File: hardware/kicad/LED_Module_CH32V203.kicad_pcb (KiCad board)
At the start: 2 copper layers, 40 x 40 mm, 97 parts, among them J1 USB_C_Receptacle_USB2.0_16P, J2 Solder Pad, J3 Qwiic / StemmaQT Connector, J4 noknok_FlashPads_USB-module, Q1 AO3401A, Q2 MMBT3904, U1 CH32V203G6U6, U2 BL9110-330BPFB (LCSC C169246), U3 SN74AHCT1G125DBVR (LCSC C7484), Y1 Crystal

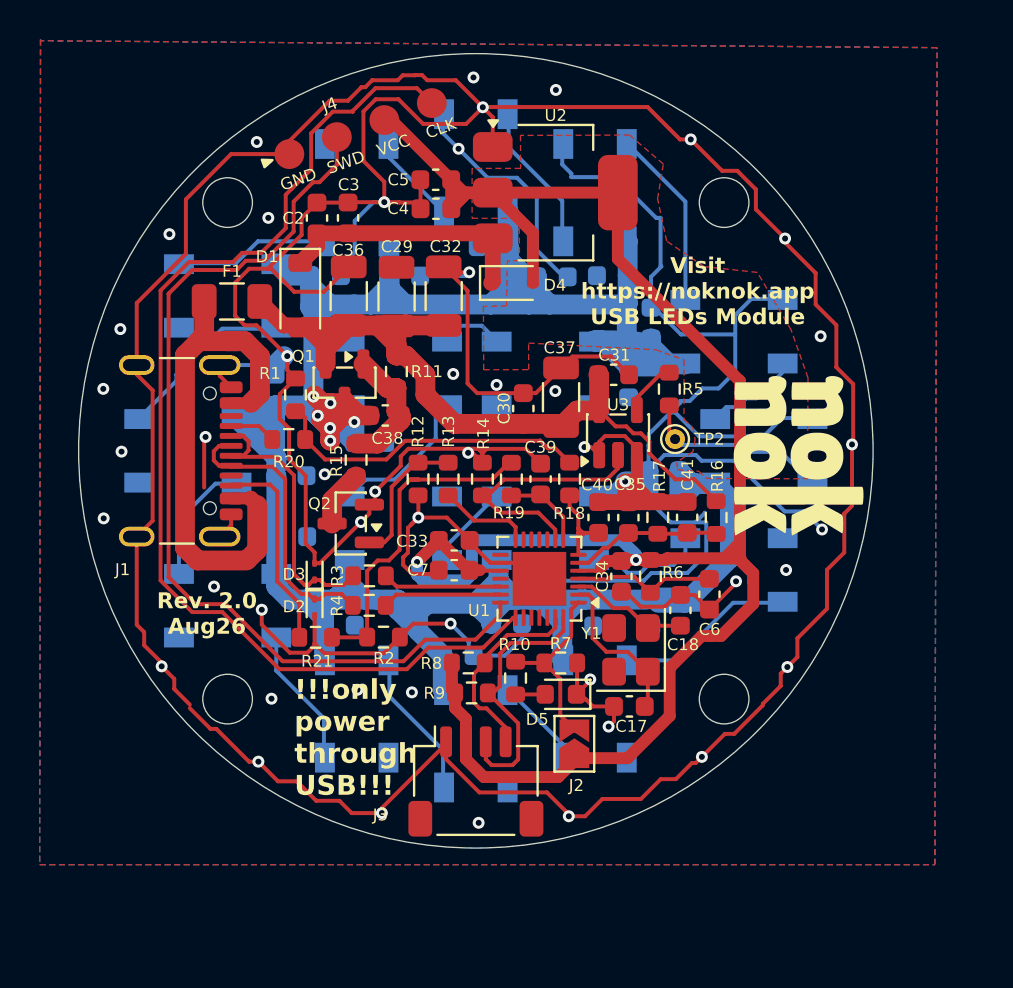
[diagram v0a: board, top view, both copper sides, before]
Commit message: hardware: revert to the 8x WS2812b board - the 16x SK6812 rev2 design moves to module-usb-led-16x
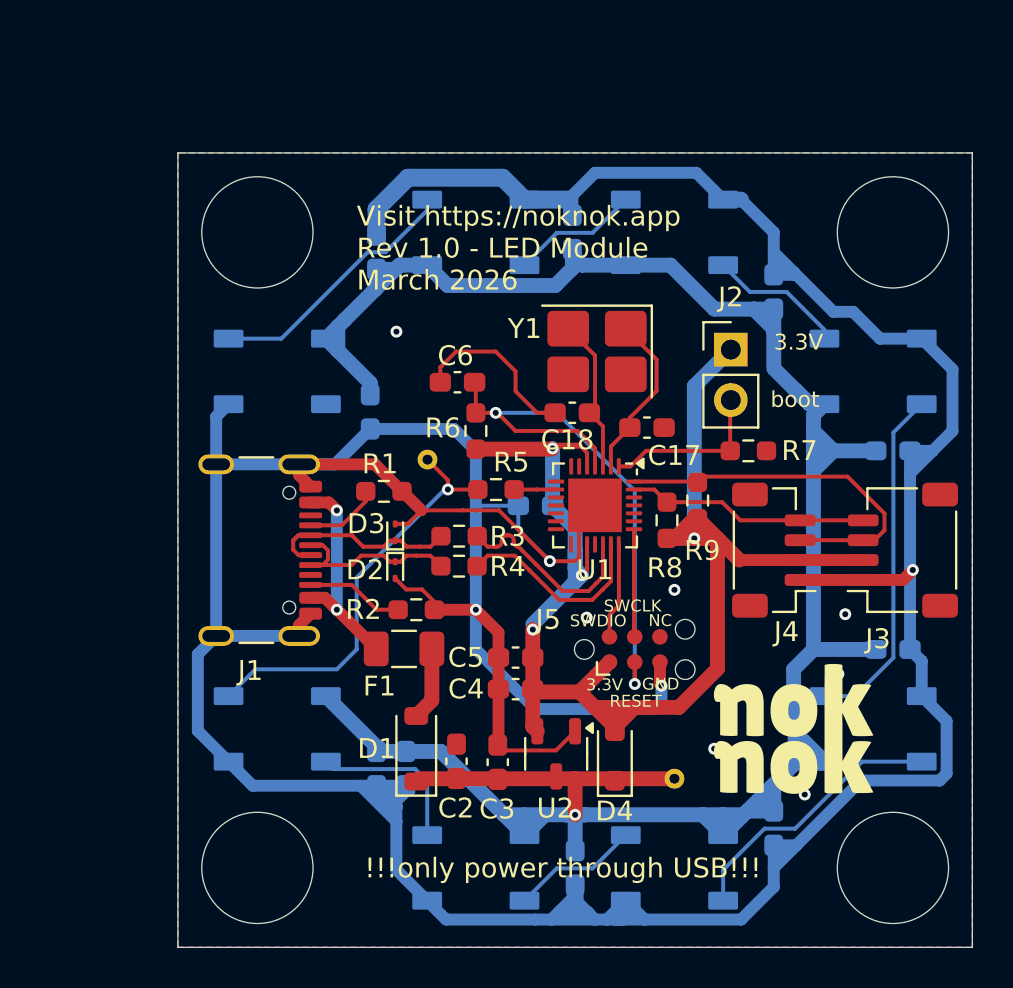
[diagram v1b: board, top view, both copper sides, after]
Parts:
- removed C19, C24: 10uF, Capacitor_SMD:C_0603_1608Metric
- removed C20, C21, C22, C23, C27, C28, C33, C34, C35, C38: 0.1uF, Capacitor_SMD:C_0603_1608Metric
- removed C29, C32, C36, C37: 22µF 25V X5R, Capacitor_SMD:C_1206_3216Metric
- removed C30, C39, C40, C41: 0.1uF X7R Ceramic, Capacitor_SMD:C_0603_1608Metric
- removed C31: 0.1uF X7R 16V+, Capacitor_SMD:C_0603_1608Metric
- removed D17, D18, D19, D20, D21, D22, D23, D24: SK6812, LED_SMD:LED_SK6812_PLCC4_5.0x5.0mm_P3.2mm
- removed D5: LED, LED_SMD:LED_0603_1608Metric
- removed H1, H2, H3: noknok_MountingHole, noknok:noknok_MountingHole_2.5mm_M2.5
- removed Q1: AO3401A, Package_TO_SOT_SMD:SOT-23
- removed Q2: MMBT3904, Package_TO_SOT_SMD:SOT-23
- removed R10: 2.2k, Resistor_SMD:R_0603_1608Metric
- removed R11, R12, R13, R14: 10k, Resistor_SMD:R_0603_1608Metric
- removed R15: 1k, Resistor_SMD:R_0603_1608Metric
- removed R16, R17: 22k, Resistor_SMD:R_0603_1608Metric
- removed R18, R19: 4.7k (1% tolerance), Resistor_SMD:R_0603_1608Metric
- removed R20, R21: 3.3k (1% tolerance), Resistor_SMD:R_0603_1608Metric
- removed U3: SN74AHCT1G125DBVR (LCSC C7484), Package_TO_SOT_SMD:SOT-23-5
- added J5: TagConnect_TC2030, Connector:Tag-Connect_TC2030-IDC-NL_2x03_P1.27mm_Vertical, F.Cu at (143.0, 105.0)
- added TP1: TestPoint, TestPoint:TestPoint_THTPad_D1.0mm_Drill0.5mm, B.Cu at (145.0, 111.5)
- C1, C10, C11, C12, C13, C14, C15, C16, C17, C18, C2, C3, C4, C5, C6, C8, C9: footprint Capacitor_SMD:C_0603_1608Metric -> Capacitor_SMD:C_0603_1608Metric_Pad1.08x0.95mm_HandSolder
- C7: footprint Capacitor_SMD:C_0603_1608Metric -> Capacitor_SMD:C_0603_1608Metric_Pad1.08x0.95mm_HandSolder; moved to B.Cu
- D1: value PMEG4010CEH (LCSC C193342) -> 1N4007
- D10, D11, D12, D13, D14, D15, D16, D9: value SK6812 -> WS2812B; footprint LED_SMD:LED_SK6812_PLCC4_5.0x5.0mm_P3.2mm -> LED_SMD:LED_WS2812B_PLCC4_5.0x5.0mm_P3.2mm
- D4: footprint Diode_SMD:D_SOD-323 -> Diode_SMD:D_SOD-323_HandSoldering
- F1: value Polyfuse at >= 2A -> Resettable Polyfuse
- J2: value Solder Pad -> Jumper Cap; footprint Jumper:SolderJumper-2_P1.3mm_Open_TrianglePad1.0x1.5mm -> Connector_PinHeader_2.54mm:PinHeader_1x02_P2.54mm_Vertical
- J4: value noknok_FlashPads_USB-module -> Qwiic / StemmaQT Connector; footprint noknok:noknok_FlashPads_USB-module_1x4_M2.5 -> Connector_JST:JST_SH_BM04B-SRSS-TB_1x04-1MP_P1.00mm_Vertical
- R1, R2: value 1.8k (1% tolerance) -> 5.1k; footprint Resistor_SMD:R_0603_1608Metric -> Resistor_SMD:R_0603_1608Metric_Pad0.98x0.95mm_HandSolder
- R3, R4, R5, R6, R7: footprint Resistor_SMD:R_0603_1608Metric -> Resistor_SMD:R_0603_1608Metric_Pad0.98x0.95mm_HandSolder
- R8, R9: value 3.3k -> 4.7k; footprint Resistor_SMD:R_0603_1608Metric -> Resistor_SMD:R_0603_1608Metric_Pad0.98x0.95mm_HandSolder
- TP2: moved to B.Cu
- U2: value BL9110-330BPFB (LCSC C169246) -> XC6206P332MR; footprint Package_TO_SOT_SMD:SOT-223-3_TabPin2 -> Package_TO_SOT_SMD:SOT-23-3
- Y1: footprint Crystal:Crystal_SMD_3225-4Pin_3.2x2.5mm -> Crystal:Crystal_SMD_3225-4Pin_3.2x2.5mm_HandSoldering
- moved D12 34.8 mm to (155.0, 109.0), turned to 0 degrees
- moved D11 34.2 mm to (145.0, 116.0), turned to 180 degrees
- moved J4 32.6 mm to (150.0, 100.0), turned to 90 degrees
- moved D10 30.0 mm to (135.0, 116.0)
- moved C11 29.0 mm to (150.0, 114.0), turned to -90 degrees
- moved C12 28.6 mm to (156.0, 105.0), turned to 0 degrees
- moved C3 28.4 mm to (136.1, 110.7)
- moved U2 28.3 mm to (139.0, 110.3), turned to -90 degrees
- moved C2 28.2 mm to (134.0, 110.6)
- moved D9 28.2 mm to (125.0, 109.0)
- moved C10 27.7 mm to (140.0, 116.0), turned to -90 degrees
- moved D13 27.5 mm to (155.0, 91.0), turned to 0 degrees
- moved C4 24.5 mm to (137.0, 107.0)
- moved J3 24.5 mm to (156.5, 100.0), turned to 90 degrees
- moved C5 24.4 mm to (137.0, 105.4)
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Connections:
- C1 pad 1: +5V_LED -> +4.1V
- C10 pad 1: +5V_LED -> +4.1V
- C11 pad 1: +5V_LED -> +4.1V
- C12 pad 1: +5V_LED -> +4.1V
- C13 pad 1: +5V_LED -> +4.1V
- C14 pad 1: +5V_LED -> +4.1V
- C15 pad 1: +5V_LED -> +4.1V
- C16 pad 1: +5V_LED -> +4.1V
- C2 pad 1: +4.65V -> +4.1V
- C3 pad 1: +4.65V -> +4.1V
- C8 pad 1: +5V_LED -> +4.1V
- C9 pad 1: +5V_LED -> +4.1V
- D1 pad 1: +4.65V -> +4.1V
- D10 pad 1: GND -> +4.1V
- D10 pad 2: Net-(D10-DIN) -> Net-(D10-DOUT)
- D10 pad 3: +5V_LED -> GND
- D10 pad 4: Net-(D10-DOUT) -> Net-(D10-DIN)
- D11 pad 1: GND -> +4.1V
- D11 pad 2: Net-(D10-DOUT) -> Net-(D11-DOUT)
- D11 pad 3: +5V_LED -> GND
- D11 pad 4: Net-(D11-DOUT) -> Net-(D10-DOUT)
- D12 pad 1: GND -> +4.1V
- D12 pad 2: Net-(D11-DOUT) -> Net-(D12-DOUT)
- D12 pad 3: +5V_LED -> GND
- D12 pad 4: Net-(D12-DOUT) -> Net-(D11-DOUT)
- D13 pad 1: GND -> +4.1V
- D13 pad 2: Net-(D12-DOUT) -> Net-(D13-DOUT)
- D13 pad 3: +5V_LED -> GND
- D13 pad 4: Net-(D13-DOUT) -> Net-(D12-DOUT)
- D14 pad 1: GND -> +4.1V
- D14 pad 2: Net-(D13-DOUT) -> Net-(D14-DOUT)
- D14 pad 3: +5V_LED -> GND
- D14 pad 4: Net-(D14-DOUT) -> Net-(D13-DOUT)
- D15 pad 1: GND -> +4.1V
- D15 pad 2: Net-(D14-DOUT) -> Net-(D15-DOUT)
- D15 pad 3: +5V_LED -> GND
- D15 pad 4: Net-(D15-DOUT) -> Net-(D14-DOUT)
- D16 pad 1: GND -> +4.1V
- D16 pad 2: Net-(D15-DOUT) -> unconnected-(D16-DOUT-Pad2)
- D16 pad 3: +5V_LED -> GND
- D16 pad 4: Net-(D16-DOUT) -> Net-(D15-DOUT)
- D4 pad 1: +4.65V -> +4.1V
- D9 pad 1: GND -> +4.1V
- D9 pad 2: /D9_DIN -> Net-(D10-DIN)
- D9 pad 3: +5V_LED -> GND
- D9 pad 4: Net-(D10-DIN) -> Net-(D9-DIN)
- J4 pad 2: Net-(J4-SWDIO) -> +3.3V
- J4 pad 3: +3.3V -> Net-(J3-Pin_3)
- J4 pad 4: Net-(J4-SWCLK) -> Net-(J3-Pin_4)
- R1 pad 2: Net-(R1-Pad2) -> Net-(J1-CC1)
- R2 pad 2: Net-(R19-Pad2) -> Net-(J1-CC2)
- R3 pad 1: D_N -> D-
- R4 pad 1: D_P -> D+
- R5 pad 1: /D9_DIN -> Net-(D9-DIN)
- R5 pad 2: Net-(R5-Pad2) -> Net-(U1-PA3)
- TP2 pad 1: /D9_DIN -> Net-(D9-DIN)
- U1 pad 14: /MCU_PB0 -> unconnected-(U1-PB0-Pad14)
- U1 pad 19: D_N -> D-
- U1 pad 20: D_P -> D+
- U1 pad 21: Net-(J4-SWDIO) -> Net-(J5-SWDIO)
- U1 pad 22: Net-(J4-SWCLK) -> Net-(J5-SWCLK)
- U1 pad 6: /MCU_PA0 -> unconnected-(U1-PA0-Pad6)
- U1 pad 7: /MCU_PA1 -> unconnected-(U1-PA1-Pad7)
- U1 pad 8: /MCU_PA2 -> unconnected-(U1-PA2-Pad8)
- U1 pad 9: /MCU_PA3 -> Net-(U1-PA3)
- U2 pad 3: +4.65V -> +4.1V
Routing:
- net +5V_LED: track 164.9 -> 0.00 mm, vias 6 -> 0
- net +4.1V: track 0.00 -> 128.9 mm, vias 0 -> 1
- net GND: track 375.6 -> 248.2 mm, vias 47 -> 11
- net Net-(J4-SWCLK): track 55.6 -> 0.00 mm
- net Net-(J4-SWDIO): track 47.8 -> 0.00 mm
- net +5V: track 43.5 -> 3.70 mm
- net +3.3V: track 102.1 -> 74.6 mm, vias 2 -> 4
- net Net-(J5-~{RESET}): track 7.29 -> 28.7 mm, vias 0 -> 2
- net Net-(D9-DIN): track 0.00 -> 20.9 mm, vias 0 -> 1
- net Net-(F1-Pad2): track 28.3 -> 10.9 mm, vias 0 -> 2
- net Net-(R19-Pad2): track 16.8 -> 0.00 mm
- net Net-(R1-Pad2): track 16.1 -> 0.00 mm
- net Net-(D12-DOUT): track 4.52 -> 17.6 mm
- net +4.65V: track 13.1 -> 0.00 mm
- net /MCU_PA3: track 12.9 -> 0.00 mm
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- removed copper zone on F.Cu, net +3.3V
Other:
- outline, holes or cut-outs redrawn
- board text added: "3.3V"
- board text added: "GND"
- board text added: "NC"
- board text added: "RESET"
- board text added: "SWCLK"
- board text added: "SWDIO"
- board text added: "Visit https://noknok.app Rev 1.0 - LED Module March 2026"
- board text added: "boot"
- board text removed: "Rev. 2.0 Aug26"
- board text removed: "Visit https://noknok.app USB LEDs Module"

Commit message: hardware: rev 2.0 round board with 16x SKC6812RGBW, add BOM and schematic PDF, drop stale renders
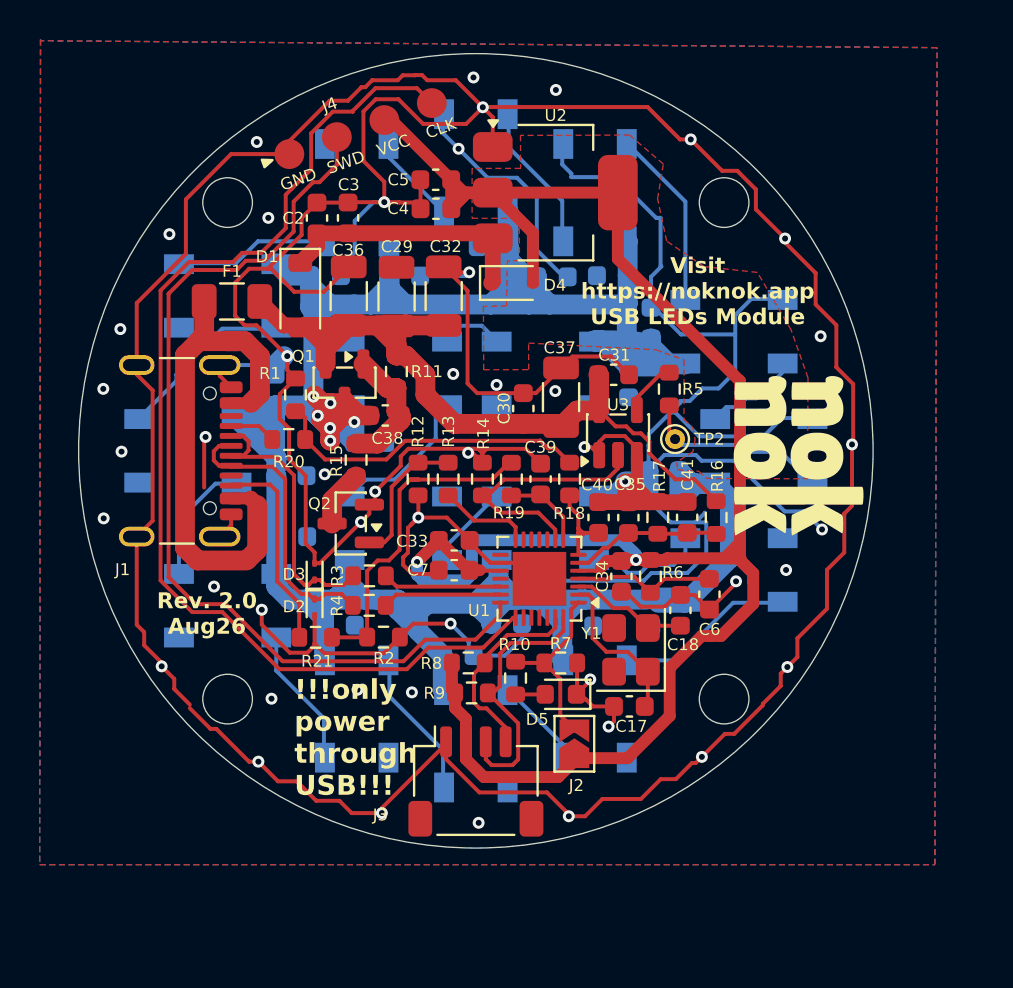
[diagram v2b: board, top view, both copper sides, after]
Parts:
- removed J5: TagConnect_TC2030, Connector:Tag-Connect_TC2030-IDC-NL_2x03_P1.27mm_Vertical
- removed TP1: TestPoint, TestPoint:TestPoint_THTPad_D1.0mm_Drill0.5mm
- added C19: 10uF, Capacitor_SMD:C_0603_1608Metric, B.Cu at (125.7, 96.2)
- added C20: 0.1uF, Capacitor_SMD:C_0603_1608Metric, B.Cu at (128.1, 103.8)
- added C21: 0.1uF, Capacitor_SMD:C_0603_1608Metric, B.Cu at (134.1, 105.3)
- added C22: 0.1uF, Capacitor_SMD:C_0603_1608Metric, B.Cu at (140.1, 103.8)
- added C23: 0.1uF, Capacitor_SMD:C_0603_1608Metric, B.Cu at (143.8, 103.1)
- added C24: 10uF, Capacitor_SMD:C_0603_1608Metric, B.Cu at (138.8, 86.2)
- added C27: 0.1uF, Capacitor_SMD:C_0603_1608Metric, B.Cu at (129.7, 94.6)
- added C28: 0.1uF, Capacitor_SMD:C_0603_1608Metric, B.Cu at (142.7, 91.5)
- added C29: 22µF 25V X5R, Capacitor_SMD:C_1206_3216Metric, F.Cu at (131.0, 87.2)
- added C30: 0.1uF X7R Ceramic, Capacitor_SMD:C_0603_1608Metric, F.Cu at (137.4, 92.9)
- added C31: 0.1uF X7R 16V+, Capacitor_SMD:C_0603_1608Metric, F.Cu at (141.9, 91.2)
- added C32: 22µF 25V X5R, Capacitor_SMD:C_1206_3216Metric, F.Cu at (133.4, 87.2)
- added C33: 0.1uF, Capacitor_SMD:C_0603_1608Metric, F.Cu at (133.9, 99.5)
- added C34: 0.1uF, Capacitor_SMD:C_0603_1608Metric, F.Cu at (142.3, 101.3)
- added C35: 0.1uF, Capacitor_SMD:C_0603_1608Metric, F.Cu at (142.7, 98.4)
- added C36: 22µF 25V X5R, Capacitor_SMD:C_1206_3216Metric, F.Cu at (128.6, 87.2)
- added C37: 22µF 25V X5R, Capacitor_SMD:C_1206_3216Metric, F.Cu at (139.3, 92.3)
- added C38: 0.1uF, Capacitor_SMD:C_0603_1608Metric, F.Cu at (130.4, 93.2)
- added C39: 0.1uF X7R Ceramic, Capacitor_SMD:C_0603_1608Metric, F.Cu at (138.3, 96.4)
- added C40: 0.1uF X7R Ceramic, Capacitor_SMD:C_0603_1608Metric, F.Cu at (141.2, 98.4)
- added C41: 0.1uF X7R Ceramic, Capacitor_SMD:C_0603_1608Metric, F.Cu at (145.6, 98.3)
- added D17: SK6812, LED_SMD:LED_SK6812_PLCC4_5.0x5.0mm_P3.2mm, B.Cu at (129.0, 108.0)
- added D18: SK6812, LED_SMD:LED_SK6812_PLCC4_5.0x5.0mm_P3.2mm, B.Cu at (135.0, 109.5)
- added D19: SK6812, LED_SMD:LED_SK6812_PLCC4_5.0x5.0mm_P3.2mm, B.Cu at (141.0, 108.0)
- added D20: SK6812, LED_SMD:LED_SK6812_PLCC4_5.0x5.0mm_P3.2mm, B.Cu at (148.0, 101.0)
- added D21: SK6812, LED_SMD:LED_SK6812_PLCC4_5.0x5.0mm_P3.2mm, B.Cu at (138.5, 98.9)
- added D22: SK6812, LED_SMD:LED_SK6812_PLCC4_5.0x5.0mm_P3.2mm, B.Cu at (131.1, 98.9)
- added D23: SK6812, LED_SMD:LED_SK6812_PLCC4_5.0x5.0mm_P3.2mm, B.Cu at (131.1, 91.1)
- added D24: SK6812, LED_SMD:LED_SK6812_PLCC4_5.0x5.0mm_P3.2mm, B.Cu at (138.5, 91.1)
- added D5: LED, LED_SMD:LED_0603_1608Metric, F.Cu at (139.3, 107.3)
- added H1: noknok_MountingHole, noknok:noknok_MountingHole_2.5mm_M2.5, F.Cu at (122.5, 107.5)
- added H2: noknok_MountingHole, noknok:noknok_MountingHole_2.5mm_M2.5, F.Cu at (147.5, 107.5)
- added H3: noknok_MountingHole, noknok:noknok_MountingHole_2.5mm_M2.5, F.Cu at (147.5, 82.5)
- added Q1: AO3401A, Package_TO_SOT_SMD:SOT-23, F.Cu at (128.4, 91.6)
- added Q2: MMBT3904, Package_TO_SOT_SMD:SOT-23, F.Cu at (128.7, 98.7)
- added R10: 2.2k, Resistor_SMD:R_0603_1608Metric, F.Cu at (137.0, 106.4)
- added R11: 10k, Resistor_SMD:R_0603_1608Metric, F.Cu at (131.0, 91.0)
- added R12: 10k, Resistor_SMD:R_0603_1608Metric, F.Cu at (132.1, 96.4)
- added R13: 10k, Resistor_SMD:R_0603_1608Metric, F.Cu at (133.6, 96.4)
- added R14: 10k, Resistor_SMD:R_0603_1608Metric, F.Cu at (135.3, 96.4)
- added R15: 1k, Resistor_SMD:R_0603_1608Metric, F.Cu at (129.0, 95.5)
- added R16: 22k, Resistor_SMD:R_0603_1608Metric, F.Cu at (147.1, 98.4)
- added R17: 22k, Resistor_SMD:R_0603_1608Metric, F.Cu at (144.2, 98.3)
- added R18: 4.7k (1% tolerance), Resistor_SMD:R_0603_1608Metric, F.Cu at (139.7, 96.4)
- added R19: 4.7k (1% tolerance), Resistor_SMD:R_0603_1608Metric, F.Cu at (136.8, 96.4)
- added R20: 3.3k (1% tolerance), Resistor_SMD:R_0603_1608Metric, F.Cu at (125.6, 94.4)
- added R21: 3.3k (1% tolerance), Resistor_SMD:R_0603_1608Metric, F.Cu at (126.9, 104.4)
- added U3: SN74AHCT1G125DBVR (LCSC C7484), Package_TO_SOT_SMD:SOT-23-5, F.Cu at (142.2, 94.1)
- C1, C10, C11, C12, C13, C14, C15, C16, C17, C18, C2, C3, C4, C5, C6, C8, C9: footprint Capacitor_SMD:C_0603_1608Metric_Pad1.08x0.95mm_HandSolder -> Capacitor_SMD:C_0603_1608Metric
- C7: footprint Capacitor_SMD:C_0603_1608Metric_Pad1.08x0.95mm_HandSolder -> Capacitor_SMD:C_0603_1608Metric; moved to F.Cu
- D1: value 1N4007 -> PMEG4010CEH (LCSC C193342)
- D10, D11, D12, D13, D14, D15, D16, D9: value WS2812B -> SK6812; footprint LED_SMD:LED_WS2812B_PLCC4_5.0x5.0mm_P3.2mm -> LED_SMD:LED_SK6812_PLCC4_5.0x5.0mm_P3.2mm
- D4: footprint Diode_SMD:D_SOD-323_HandSoldering -> Diode_SMD:D_SOD-323
- F1: value Resettable Polyfuse -> Polyfuse at >= 2A
- J2: value Jumper Cap -> Solder Pad; footprint Connector_PinHeader_2.54mm:PinHeader_1x02_P2.54mm_Vertical -> Jumper:SolderJumper-2_P1.3mm_Open_TrianglePad1.0x1.5mm
- J4: value Qwiic / StemmaQT Connector -> noknok_FlashPads_USB-module; footprint Connector_JST:JST_SH_BM04B-SRSS-TB_1x04-1MP_P1.00mm_Vertical -> noknok:noknok_FlashPads_USB-module_1x4_M2.5
- R1, R2: value 5.1k -> 1.8k (1% tolerance); footprint Resistor_SMD:R_0603_1608Metric_Pad0.98x0.95mm_HandSolder -> Resistor_SMD:R_0603_1608Metric
- R3, R4, R5, R6, R7: footprint Resistor_SMD:R_0603_1608Metric_Pad0.98x0.95mm_HandSolder -> Resistor_SMD:R_0603_1608Metric
- R8, R9: value 4.7k -> 3.3k; footprint Resistor_SMD:R_0603_1608Metric_Pad0.98x0.95mm_HandSolder -> Resistor_SMD:R_0603_1608Metric
- TP2: moved to F.Cu
- U2: value XC6206P332MR -> BL9110-330BPFB (LCSC C169246); footprint Package_TO_SOT_SMD:SOT-23-3 -> Package_TO_SOT_SMD:SOT-223-3_TabPin2
- Y1: footprint Crystal:Crystal_SMD_3225-4Pin_3.2x2.5mm_HandSoldering -> Crystal:Crystal_SMD_3225-4Pin_3.2x2.5mm
- moved D12 34.8 mm to (135.0, 80.5), turned to -90 degrees
- moved D11 34.2 mm to (141.0, 82.0), turned to -90 degrees
- moved J4 32.6 mm to (122.5, 82.5), turned to 19.7 degrees
- moved D10 30.0 mm to (148.0, 89.0)
- moved C11 29.0 mm to (141.9, 86.2), turned to 180 degrees
- moved C12 28.6 mm to (135.9, 84.7), turned to 180 degrees
- moved C3 28.4 mm to (128.6, 83.3)
- moved U2 28.3 mm to (139.0, 82.0), turned to 0 degrees
- moved C2 28.2 mm to (127.0, 83.3)
- moved D9 28.2 mm to (149.5, 95.0)
- moved C10 27.7 mm to (143.8, 88.6), turned to 90 degrees
- moved D13 27.5 mm to (129.0, 82.0), turned to -90 degrees
- moved C4 24.5 mm to (133.0, 82.8)
- moved J3 24.5 mm to (135.0, 111.7), turned to 0 degrees
- moved C5 24.4 mm to (133.0, 81.3)
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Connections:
- C1 pad 1: +4.1V -> +5V_LED
- C10 pad 1: +4.1V -> +5V_LED
- C11 pad 1: +4.1V -> +5V_LED
- C12 pad 1: +4.1V -> +5V_LED
- C13 pad 1: +4.1V -> +5V_LED
- C14 pad 1: +4.1V -> +5V_LED
- C15 pad 1: +4.1V -> +5V_LED
- C16 pad 1: +4.1V -> +5V_LED
- C2 pad 1: +4.1V -> +4.65V
- C3 pad 1: +4.1V -> +4.65V
- C8 pad 1: +4.1V -> +5V_LED
- C9 pad 1: +4.1V -> +5V_LED
- D1 pad 1: +4.1V -> +4.65V
- D10 pad 1: +4.1V -> GND
- D10 pad 2: Net-(D10-DOUT) -> Net-(D10-DIN)
- D10 pad 3: GND -> +5V_LED
- D10 pad 4: Net-(D10-DIN) -> Net-(D10-DOUT)
- D11 pad 1: +4.1V -> GND
- D11 pad 2: Net-(D11-DOUT) -> Net-(D10-DOUT)
- D11 pad 3: GND -> +5V_LED
- D11 pad 4: Net-(D10-DOUT) -> Net-(D11-DOUT)
- D12 pad 1: +4.1V -> GND
- D12 pad 2: Net-(D12-DOUT) -> Net-(D11-DOUT)
- D12 pad 3: GND -> +5V_LED
- D12 pad 4: Net-(D11-DOUT) -> Net-(D12-DOUT)
- D13 pad 1: +4.1V -> GND
- D13 pad 2: Net-(D13-DOUT) -> Net-(D12-DOUT)
- D13 pad 3: GND -> +5V_LED
- D13 pad 4: Net-(D12-DOUT) -> Net-(D13-DOUT)
- D14 pad 1: +4.1V -> GND
- D14 pad 2: Net-(D14-DOUT) -> Net-(D13-DOUT)
- D14 pad 3: GND -> +5V_LED
- D14 pad 4: Net-(D13-DOUT) -> Net-(D14-DOUT)
- D15 pad 1: +4.1V -> GND
- D15 pad 2: Net-(D15-DOUT) -> Net-(D14-DOUT)
- D15 pad 3: GND -> +5V_LED
- D15 pad 4: Net-(D14-DOUT) -> Net-(D15-DOUT)
- D16 pad 1: +4.1V -> GND
- D16 pad 2: unconnected-(D16-DOUT-Pad2) -> Net-(D15-DOUT)
- D16 pad 3: GND -> +5V_LED
- D16 pad 4: Net-(D15-DOUT) -> Net-(D16-DOUT)
- D4 pad 1: +4.1V -> +4.65V
- D9 pad 1: +4.1V -> GND
- D9 pad 2: Net-(D10-DIN) -> /D9_DIN
- D9 pad 3: GND -> +5V_LED
- D9 pad 4: Net-(D9-DIN) -> Net-(D10-DIN)
- J4 pad 2: +3.3V -> Net-(J4-SWDIO)
- J4 pad 3: Net-(J3-Pin_3) -> +3.3V
- J4 pad 4: Net-(J3-Pin_4) -> Net-(J4-SWCLK)
- R1 pad 2: Net-(J1-CC1) -> Net-(R1-Pad2)
- R2 pad 2: Net-(J1-CC2) -> Net-(R19-Pad2)
- R3 pad 1: D- -> D_N
- R4 pad 1: D+ -> D_P
- R5 pad 1: Net-(D9-DIN) -> /D9_DIN
- R5 pad 2: Net-(U1-PA3) -> Net-(R5-Pad2)
- TP2 pad 1: Net-(D9-DIN) -> /D9_DIN
- U1 pad 14: unconnected-(U1-PB0-Pad14) -> /MCU_PB0
- U1 pad 19: D- -> D_N
- U1 pad 20: D+ -> D_P
- U1 pad 21: Net-(J5-SWDIO) -> Net-(J4-SWDIO)
- U1 pad 22: Net-(J5-SWCLK) -> Net-(J4-SWCLK)
- U1 pad 6: unconnected-(U1-PA0-Pad6) -> /MCU_PA0
- U1 pad 7: unconnected-(U1-PA1-Pad7) -> /MCU_PA1
- U1 pad 8: unconnected-(U1-PA2-Pad8) -> /MCU_PA2
- U1 pad 9: Net-(U1-PA3) -> /MCU_PA3
- U2 pad 3: +4.1V -> +4.65V
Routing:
- net +5V_LED: track 0.00 -> 164.9 mm, vias 0 -> 6
- net +4.1V: track 128.9 -> 0.00 mm, vias 1 -> 0
- net GND: track 248.2 -> 375.6 mm, vias 11 -> 47
- net Net-(J4-SWCLK): track 0.00 -> 55.6 mm
- net Net-(J4-SWDIO): track 0.00 -> 47.8 mm
- net +5V: track 3.70 -> 43.5 mm
- net +3.3V: track 74.6 -> 102.1 mm, vias 4 -> 2
- net Net-(U1-~{RST}): track 28.7 -> 7.29 mm, vias 2 -> 0
- net Net-(D9-DIN): track 20.9 -> 0.00 mm, vias 1 -> 0
- net Net-(F1-Pad2): track 10.9 -> 28.3 mm, vias 2 -> 0
- net Net-(R19-Pad2): track 0.00 -> 16.8 mm
- net Net-(R1-Pad2): track 0.00 -> 16.1 mm
- net Net-(D12-DOUT): track 17.6 -> 4.52 mm
- net +4.65V: track 0.00 -> 13.1 mm
- net /MCU_PA3: track 0.00 -> 12.9 mm
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- added copper zone on F.Cu, net +3.3V
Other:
- outline, holes or cut-outs redrawn
- board text added: "Rev. 2.0 Aug26"
- board text added: "Visit https://noknok.app USB LEDs Module"
- board text removed: "3.3V"
- board text removed: "GND"
- board text removed: "NC"
- board text removed: "RESET"
- board text removed: "SWCLK"
- board text removed: "SWDIO"
- board text removed: "Visit https://noknok.app Rev 1.0 - LED Module March 2026"
- board text removed: "boot"
